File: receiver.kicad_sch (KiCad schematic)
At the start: 6 parts, among them J10 Conn_01x03, J11 Conn_01x03, J12 Conn_01x03, J13 Conn_01x03, J8 Conn_01x03, J9 Conn_01x03

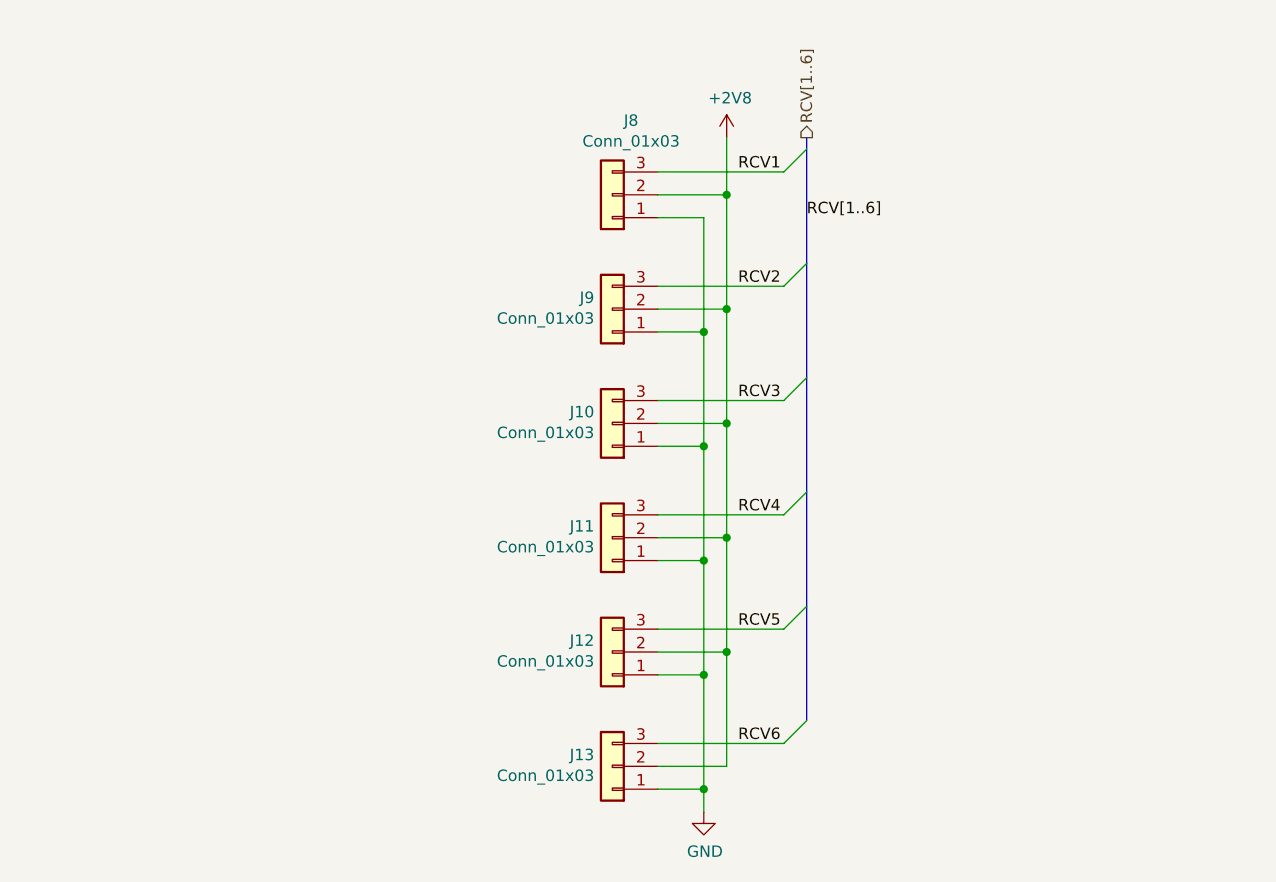
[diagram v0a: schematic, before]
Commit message: Initial schematic version
This is now a clean and ready version of the schematic:
That means:
- Schematic has been reviewed,
- It's fully annotated,
- All elements have been checked for availability with JLCPCB,
- Footprints were assigned,
- ERC is green.

No design changes should be added for this version until
the PCB is present and version is released.
Only bugfixes are possible now.
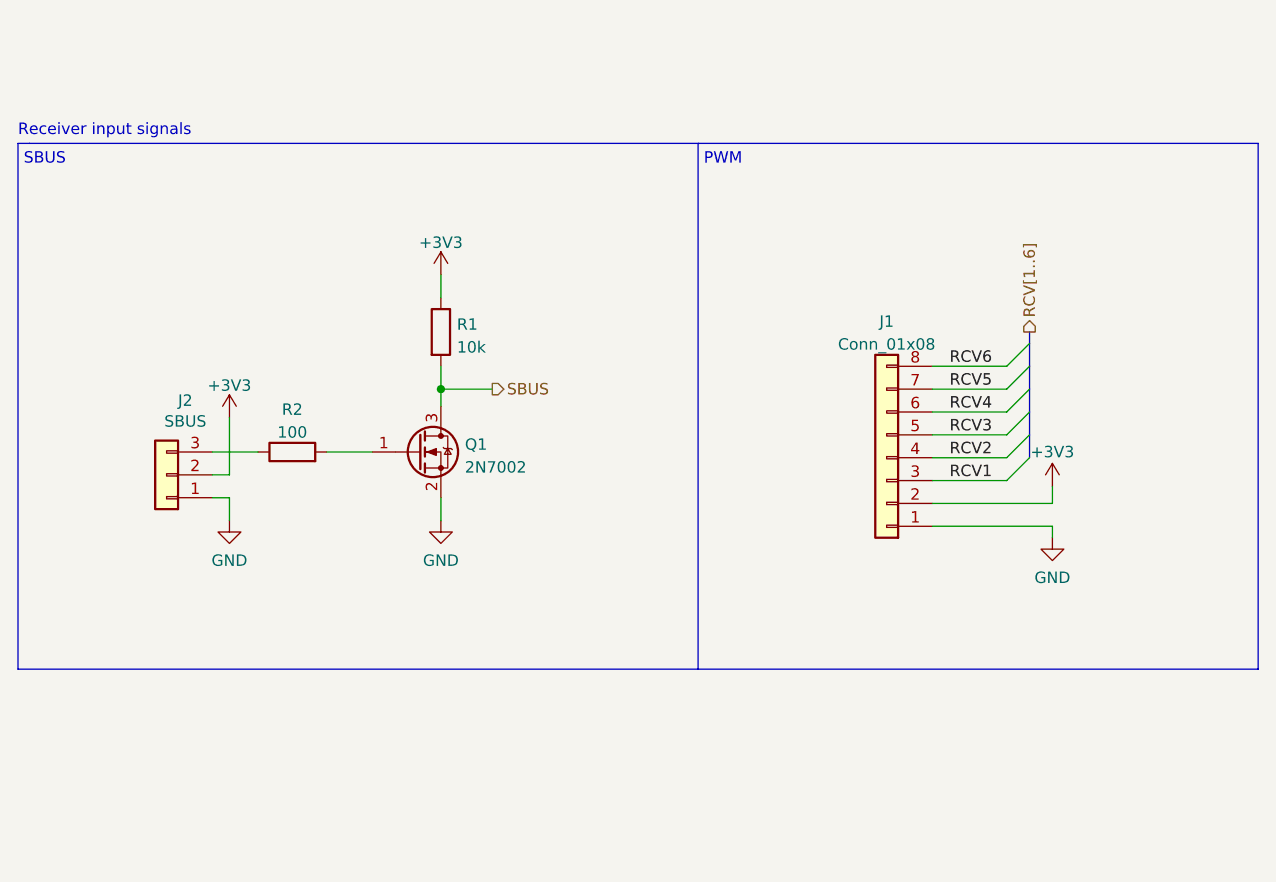
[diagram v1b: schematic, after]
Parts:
- removed J10, J11, J12, J13, J8, J9: Conn_01x03, Connector_PinHeader_2.54mm:PinHeader_1x03_P2.54mm_Vertical, symbol Connector_Generic:Conn_01x03
- added J1: Conn_01x08, Connector_PinHeader_2.54mm:PinHeader_1x08_P2.54mm_Vertical, symbol Connector_Generic:Conn_01x08
- added J2: SBUS, Connector_PinHeader_2.54mm:PinHeader_1x03_P2.54mm_Vertical, symbol Connector_Generic:Conn_01x03
- added Q1: 2N7002, Package_TO_SOT_SMD:SOT-23, symbol Transistor_FET:2N7002
- added R1: 10k, Resistor_SMD:R_0402_1005Metric, symbol Device:R
- added R2: 100, Resistor_SMD:R_0402_1005Metric, symbol Device:R
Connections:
- net GND: now also J1.1 (Pin_1), J2.1 (Pin_1), Q1.2 (S)
- net RCV1: now also J1.3 (Pin_3)
- net RCV2: now also J1.4 (Pin_4)
- net RCV3: now also J1.5 (Pin_5)
- net RCV4: now also J1.6 (Pin_6)
- net RCV5: now also J1.7 (Pin_7)
- net RCV6: now also J1.8 (Pin_8)
- new net: J2.3 (Pin_3), R2.1
- new net: Q1.1 (G), R2.2
- new net +3V3: J1.2 (Pin_2), J2.2 (Pin_2), R1.1
- new net SBUS: Q1.3 (D), R1.2
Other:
- note added: "PWM"
- note added: "Receiver input signals"
- note added: "SBUS"

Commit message: Update footprints and add JLCPCB fields
Update some footprints which will suit better building the pcb
with JLCBPCB. Add fields to components sourced from JLCPCB
to be able to generate BOM.
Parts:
- Q1: JLC (none) -> SOT-23; LCSC (none) -> C8545
- R1: JLC (none) -> 0402; LCSC (none) -> C25744
- R2: JLC (none) -> 0402; LCSC (none) -> C25076
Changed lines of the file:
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@@
       (effects (font (size 1.27 1.27)) (justify left) hide)
+    )
+    (property "JLC" "SOT-23" (id 4) (at 118.11 100.965 0)
+      (effects (font (size 1.27 1.27)) hide)
+    )
+    (property "LCSC" "C8545" (id 5) (at 118.11 100.965 0)
+      (effects (font (size 1.27 1.27)) hide)
     )
     (pin "1")
@@
     )
     (property "Datasheet" "~" (id 3) (at 104.14 100.965 0)
+      (effects (font (size 1.27 1.27)) hide)
+    )
+    (property "JLC" "0402" (id 4) (at 104.14 100.965 0)
+      (effects (font (size 1.27 1.27)) hide)
+    )
+    (property "LCSC" " C25076" (id 5) (at 104.14 100.965 0)
       (effects (font (size 1.27 1.27)) hide)
     )
@@
       (effects (font (size 1.27 1.27)) hide)
     )
+    (property "JLC" "0402" (id 4) (at 120.65 87.63 0)
+      (effects (font (size 1.27 1.27)) hide)
+    )
+    (property "LCSC" " C25744" (id 5) (at 120.65 87.63 0)
+      (effects (font (size 1.27 1.27)) hide)
+    )
